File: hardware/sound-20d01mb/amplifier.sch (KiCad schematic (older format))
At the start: 30 parts

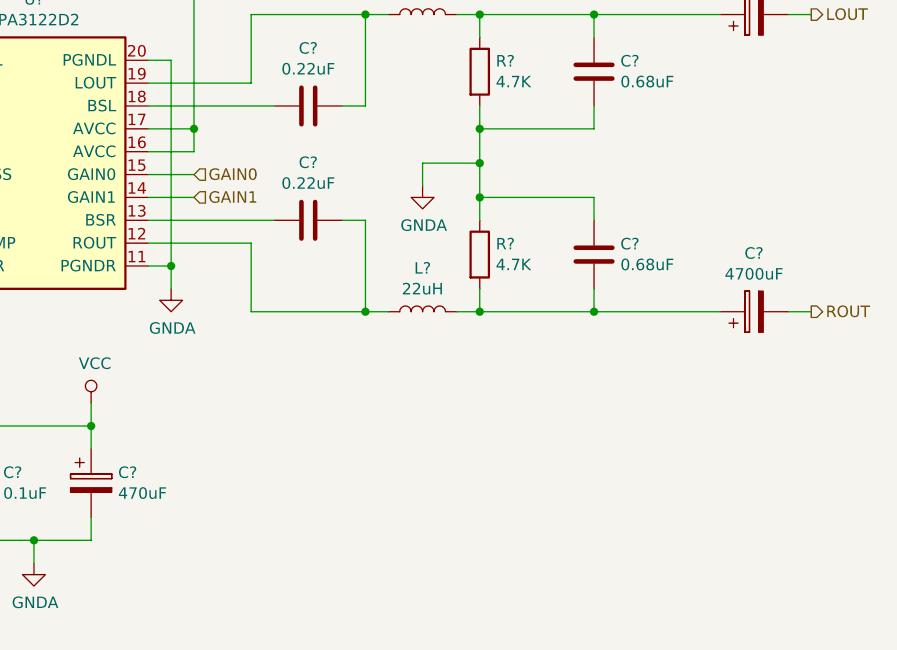
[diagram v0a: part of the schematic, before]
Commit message: Added Gain Settings
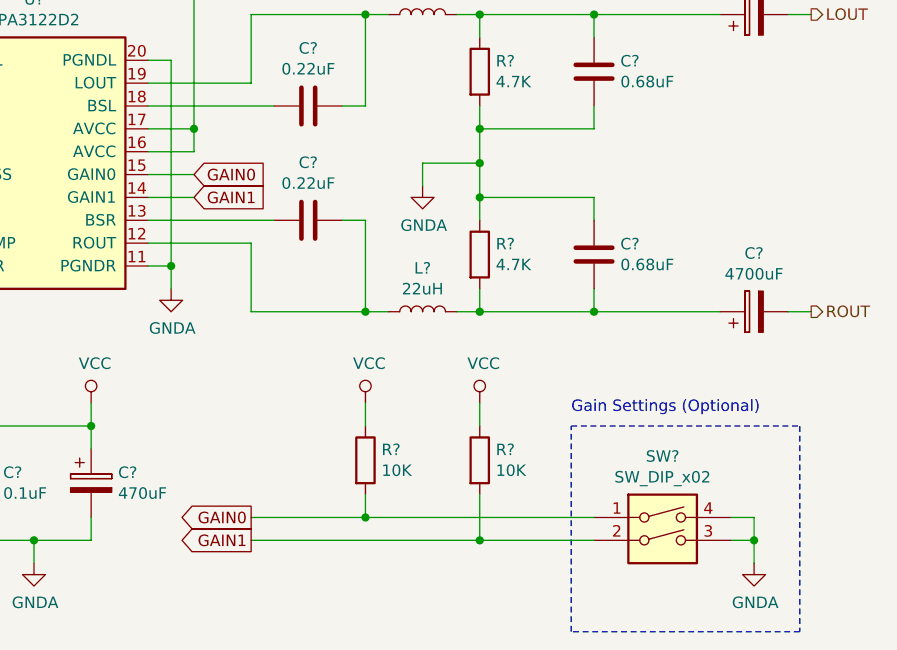
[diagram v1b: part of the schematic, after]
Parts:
- added R? (x2): 10K, Resistor_SMD:R_1206_3216Metric_Pad1.42x1.75mm_HandSolder, symbol Device:R
- added SW?: SW_DIP_x02, Button_Switch_THT:SW_DIP_SPSTx02_Slide_9.78x7.26mm_W7.62mm_P2.54mm, symbol Switch:SW_DIP_x02
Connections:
- net GAIN0: now also R?.2, SW?.1
- net GAIN1: now also R?.2, SW?.2
- net GNDA: now also SW?.3, SW?.4
- net VCC: now also R?.1, R?.1
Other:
- note added: "Gain Settings (Optional)"
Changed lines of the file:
@@
 Connection ~ 8650 2000
-Wire Wire Line
-	7450 3700 7650 3700
-Wire Wire Line
-	7450 3800 7650 3800
 Wire Wire Line
 	7450 3300 7900 3300
@@
 Wire Wire Line
 	6450 3400 6350 3400
-Text HLabel 7650 3700 2    50   Input ~ 0
-GAIN0
-Text HLabel 7650 3800 2    50   Input ~ 0
-GAIN1
 $Comp
 L sound-20d01_Library:PGA2311P U?
@@
 Text Notes 1150 1100 0    50   ~ 0
 Place power-supply bypass capacitors as\nclose to the PGA2311 package as physically possible.
+$Comp
+L Switch:SW_DIP_x02 SW?
+U 1 1 60E21294
+P 9700 5300
+F 0 "SW?" H 9700 5667 50  0000 C CNN
+F 1 "SW_DIP_x02" H 9700 5576 50  0000 C CNN
+F 2 "Button_Switch_THT:SW_DIP_SPSTx02_Slide_9.78x7.26mm_W7.62mm_P2.54mm" H 9700 5300 50  0001 C CNN
+F 3 "" H 9700 5300 50  0001 C CNN
+	1    9700 5300
+	1    0    0    -1
+$EndComp
+$Comp
+L power:GNDA #PWR?
+U 1 1 60E2143D
+P 10100 5400
+F 0 "#PWR?" H 10100 5150 50  0001 C CNN
+F 1 "GNDA" H 10105 5227 50  0000 C CNN
+F 2 "" H 10100 5400 50  0001 C CNN
+F 3 "" H 10100 5400 50  0001 C CNN
+	1    10100 5400
+	1    0    0    -1
+$EndComp
+Wire Wire Line
+	10000 5300 10100 5300
+Wire Wire Line
+	10100 5300 10100 5400
+Wire Wire Line
+	10000 5200 10100 5200
+Wire Wire Line
+	10100 5200 10100 5300
+Connection ~ 10100 5300
+$Comp
+L Device:R R?
+U 1 1 60E3F5FC
+P 8400 4950
+F 0 "R?" H 8470 4996 50  0000 L CNN
+F 1 "10K" H 8470 4905 50  0000 L CNN
+F 2 "Resistor_SMD:R_1206_3216Metric_Pad1.42x1.75mm_HandSolder" V 8330 4950 50  0001 C CNN
+F 3 "~" H 8400 4950 50  0001 C CNN
+	1    8400 4950
+	1    0    0    -1
+$EndComp
+$Comp
+L Device:R R?
+U 1 1 60E56A6D
+P 8900 4950
+F 0 "R?" H 8970 4996 50  0000 L CNN
+F 1 "10K" H 8970 4905 50  0000 L CNN
+F 2 "Resistor_SMD:R_1206_3216Metric_Pad1.42x1.75mm_HandSolder" V 8830 4950 50  0001 C CNN
+F 3 "~" H 8900 4950 50  0001 C CNN
+	1    8900 4950
+	1    0    0    -1
+$EndComp
+$Comp
+L power:VCC #PWR?
+U 1 1 60E7D456
+P 8400 4700
+F 0 "#PWR?" H 8400 4550 50  0001 C CNN
+F 1 "VCC" H 8417 4873 50  0000 C CNN
+F 2 "" H 8400 4700 50  0001 C CNN
+F 3 "" H 8400 4700 50  0001 C CNN
+	1    8400 4700
+	1    0    0    -1
+$EndComp
+Wire Wire Line
+	8400 4800 8400 4700
+$Comp
+L power:VCC #PWR?
+U 1 1 60E84FC2
+P 8900 4700
+F 0 "#PWR?" H 8900 4550 50  0001 C CNN
+F 1 "VCC" H 8917 4873 50  0000 C CNN
+F 2 "" H 8900 4700 50  0001 C CNN
+F 3 "" H 8900 4700 50  0001 C CNN
+	1    8900 4700
+	1    0    0    -1
+$EndComp
+Wire Wire Line
+	8900 4800 8900 4700
+Wire Wire Line
+	9400 5200 8400 5200
+Wire Wire Line
+	8400 5200 8400 5100
+Wire Wire Line
+	9400 5300 8900 5300
+Wire Wire Line
+	8900 5300 8900 5100
+Wire Notes Line
+	9300 4800 10300 4800
+Wire Notes Line
+	10300 4800 10300 5700
+Wire Notes Line
+	10300 5700 9300 5700
+Wire Notes Line
+	9300 5700 9300 4800
+Text Notes 9300 4750 0    50   ~ 0
+Gain Settings (Optional)
+Wire Wire Line
+	7450 3700 7650 3700
+Wire Wire Line
+	7450 3800 7650 3800
+Wire Wire Line
+	8400 5200 7900 5200
+Connection ~ 8400 5200
+Wire Wire Line
+	8900 5300 7900 5300
+Connection ~ 8900 5300
+Text GLabel 7900 5200 0    50   Output ~ 0
+GAIN0
+Text GLabel 7650 3700 2    50   Input ~ 0
+GAIN0
+Text GLabel 7900 5300 0    50   Output ~ 0
+GAIN1
+Text GLabel 7650 3800 2    50   Input ~ 0
+GAIN1
 $EndSCHEMATC

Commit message: Connected MCU to DAC
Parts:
- C? (x4): footprint (none) -> Capacitor_SMD:C_1206_3216Metric_Pad1.42x1.75mm_HandSolder
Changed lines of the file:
@@
 F 0 "C?" V 5102 3300 50  0000 C CNN
 F 1 "2.2uF" V 5011 3300 50  0000 C CNN
-F 2 "" H 4888 3150 50  0001 C CNN
+F 2 "Capacitor_SMD:C_1206_3216Metric_Pad1.42x1.75mm_HandSolder" H 4888 3150 50  0001 C CNN
 F 3 "~" H 4850 3300 50  0001 C CNN
 	1    4850 3300
@@
 F 0 "C?" V 5102 3800 50  0000 C CNN
 F 1 "2.2uF" V 5011 3800 50  0000 C CNN
-F 2 "" H 4888 3650 50  0001 C CNN
+F 2 "Capacitor_SMD:C_1206_3216Metric_Pad1.42x1.75mm_HandSolder" H 4888 3650 50  0001 C CNN
 F 3 "~" H 4850 3800 50  0001 C CNN
 	1    4850 3800
@@
 F 0 "C?" V 4152 4100 50  0000 C CNN
 F 1 "2.2uF" V 4061 4100 50  0000 C CNN
-F 2 "" H 3938 3950 50  0001 C CNN
+F 2 "Capacitor_SMD:C_1206_3216Metric_Pad1.42x1.75mm_HandSolder" H 3938 3950 50  0001 C CNN
 F 3 "~" H 3900 4100 50  0001 C CNN
 	1    3900 4100
@@
 F 0 "C?" V 4152 3000 50  0000 C CNN
 F 1 "2.2uF" V 4061 3000 50  0000 C CNN
-F 2 "" H 3938 2850 50  0001 C CNN
+F 2 "Capacitor_SMD:C_1206_3216Metric_Pad1.42x1.75mm_HandSolder" H 3938 2850 50  0001 C CNN
 F 3 "~" H 3900 3000 50  0001 C CNN
 	1    3900 3000

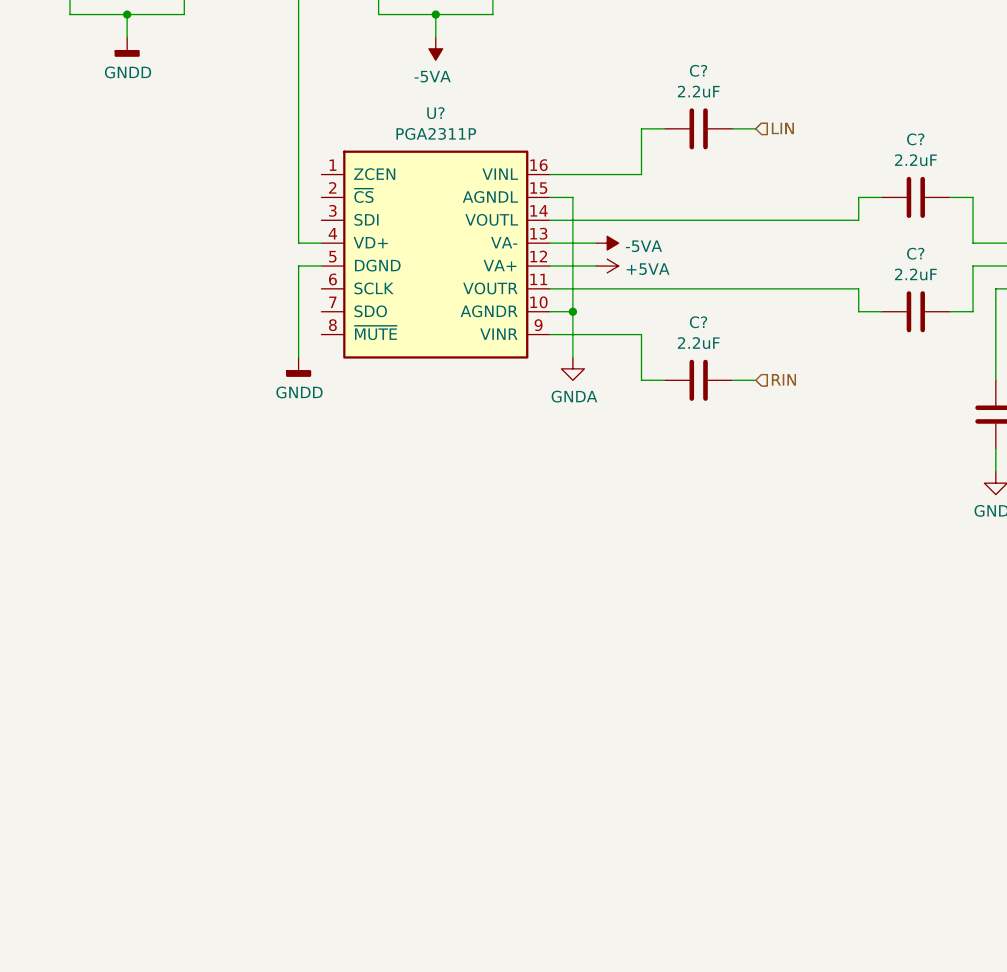
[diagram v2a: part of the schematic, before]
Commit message: Added ADG3304BRUZ
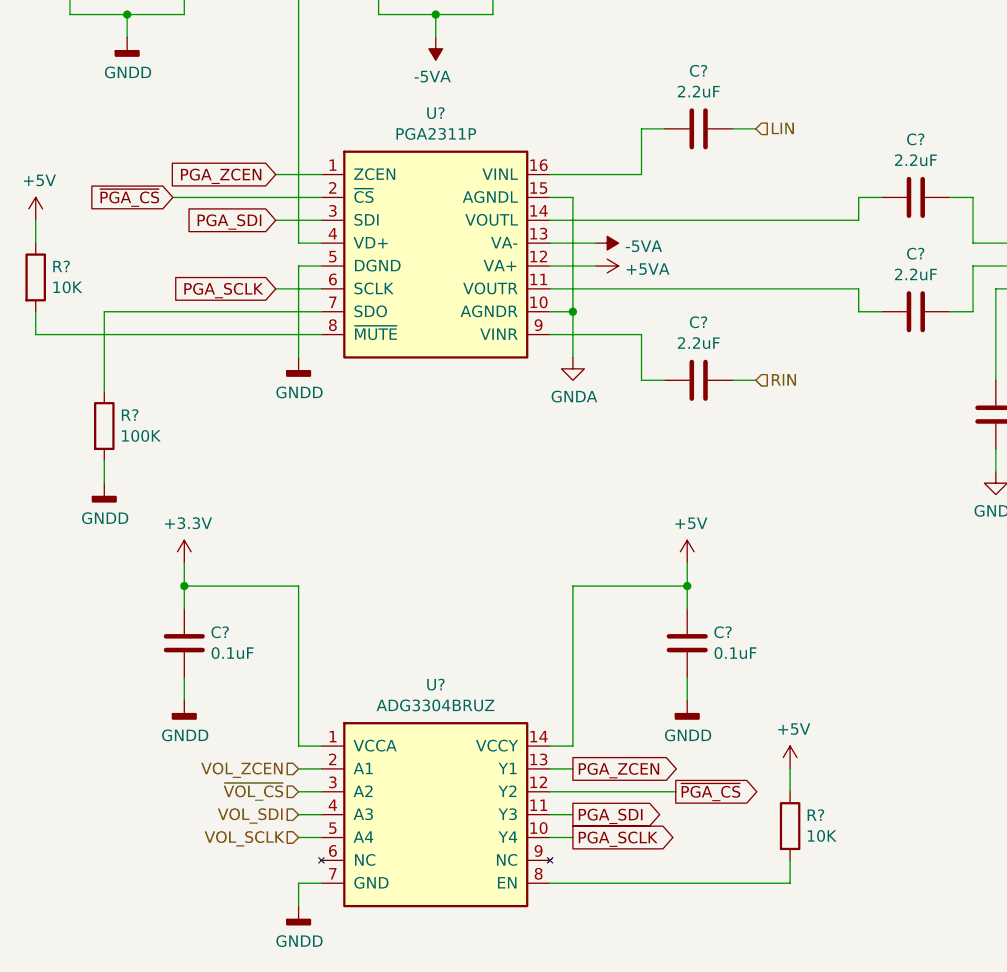
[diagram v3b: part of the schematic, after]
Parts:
- added C? (x2): 0.1uF, Capacitor_SMD:C_1206_3216Metric_Pad1.42x1.75mm_HandSolder, symbol Device:C
- added R?: 100K, Resistor_SMD:R_1206_3216Metric_Pad1.42x1.75mm_HandSolder, symbol Device:R
- added R? (x2): 10K, Resistor_SMD:R_1206_3216Metric_Pad1.42x1.75mm_HandSolder, symbol Device:R
- added U?: ADG3304BRUZ, Package_SO:TSSOP-14_4.4x5mm_P0.65mm, symbol sound-20d01_Library:ADG3304BRUZ
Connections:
- net +5V: now also C?.1, R?.1, R?.1, U?.14 (VCCY)
- net GNDD: now also C?.2, C?.2, R?.2, U?.7 (GND)
- net PGA_ZCEN: now reaches U?.1 (ZCEN)
- net PGA_ZCEN: now also U?.13 (Y1)
- net ~PGA_CS: now reaches U?.2 (~CS)
- net ~PGA_CS: now also U?.12 (Y2)
- net PGA_SDI: now reaches U?.3 (SDI)
- net PGA_SDI: now also U?.11 (Y3)
- net PGA_SCLK: now reaches U?.6 (SCLK)
- net PGA_SCLK: now also U?.10 (Y4)
- net at U?.7 (SDO): now also R?.1
- net at U?.8 (~MUTE): now also R?.2
- new net: R?.2, U?.8 (EN)
- new net +3V3: C?.1, U?.1 (VCCA)
- new net VOL_SCLK: U?.5 (A4)
- new net VOL_SDI: U?.4 (A3)
- new net VOL_ZCEN: U?.2 (A1)
- new net ~VOL_CS: U?.3 (A2)

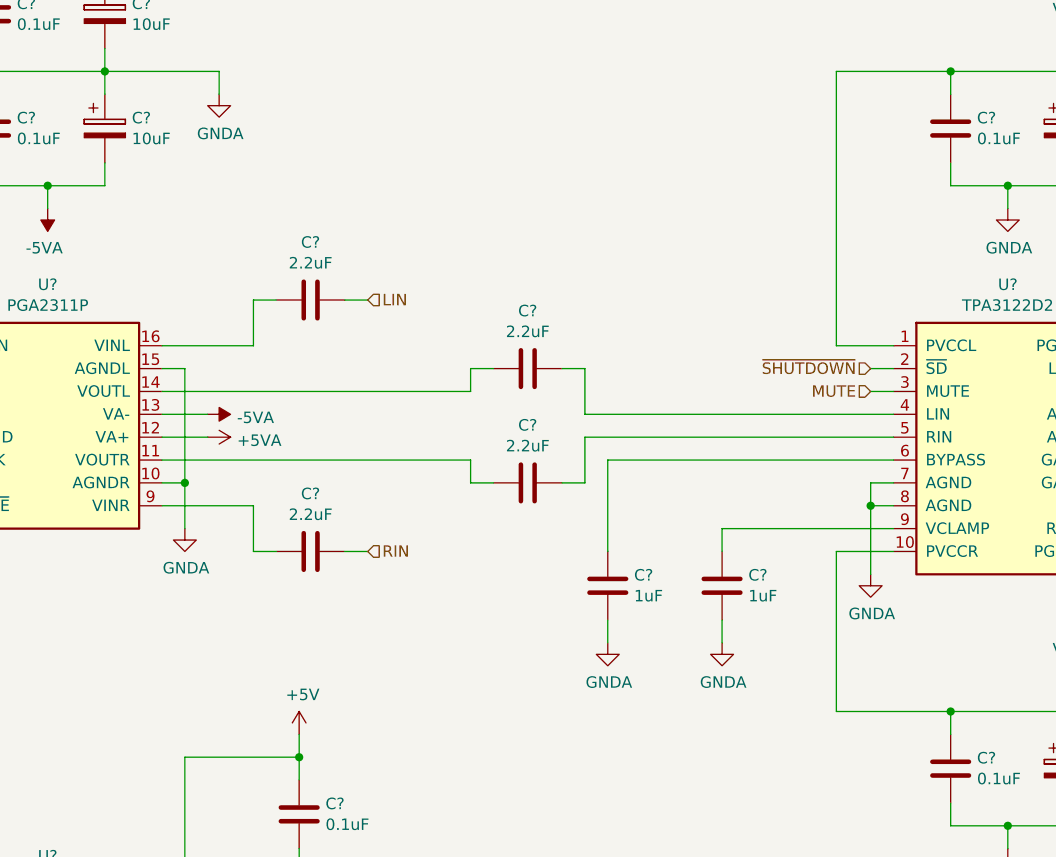
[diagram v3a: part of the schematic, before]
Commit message: Updated amplifier.sch
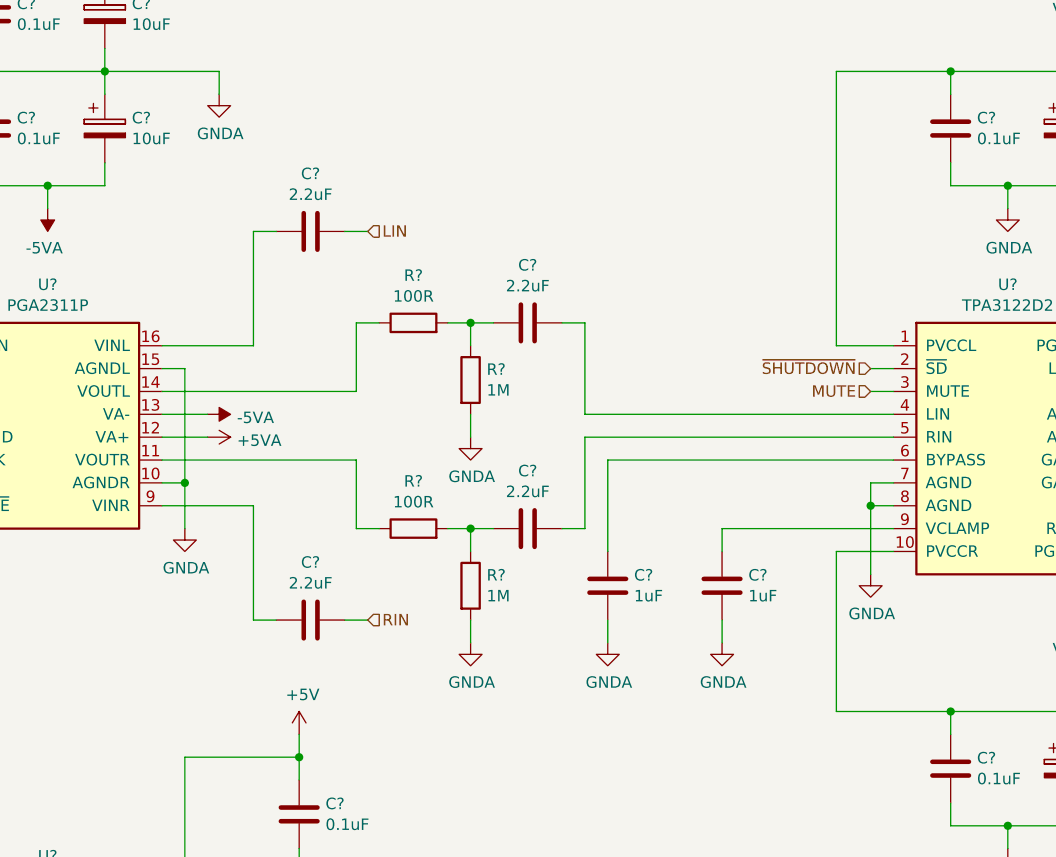
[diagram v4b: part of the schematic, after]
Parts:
- added R? (x2): 100R, Resistor_SMD:R_1206_3216Metric_Pad1.42x1.75mm_HandSolder, symbol Device:R
- added R? (x2): 1M, Resistor_SMD:R_1206_3216Metric_Pad1.42x1.75mm_HandSolder, symbol Device:R
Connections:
- net GNDA: now also R?.2, R?.2
- net at U?.11 (VOUTR): now also R?.1; no longer C?.1
- net at U?.14 (VOUTL): now also R?.1; no longer C?.1
- new net: C?.1, R?.1, R?.2 (x2)
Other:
- moved on the sheet: C?
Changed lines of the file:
@@
 L Device:C C?
 U 1 1 60E76A1B
-P 4850 3300
-F 0 "C?" V 5102 3300 50  0000 C CNN
-F 1 "2.2uF" V 5011 3300 50  0000 C CNN
-F 2 "Capacitor_SMD:C_1206_3216Metric_Pad1.42x1.75mm_HandSolder" H 4888 3150 50  0001 C CNN
-F 3 "~" H 4850 3300 50  0001 C CNN
-	1    4850 3300
+P 4850 3100
+F 0 "C?" V 5102 3100 50  0000 C CNN
+F 1 "2.2uF" V 5011 3100 50  0000 C CNN
+F 2 "Capacitor_SMD:C_1206_3216Metric_Pad1.42x1.75mm_HandSolder" H 4888 2950 50  0001 C CNN
+F 3 "~" H 4850 3100 50  0001 C CNN
+	1    4850 3100
 	0    -1   -1   0
 $EndComp
@@
 L Device:C C?
 U 1 1 60E79504
-P 4850 3800
-F 0 "C?" V 5102 3800 50  0000 C CNN
-F 1 "2.2uF" V 5011 3800 50  0000 C CNN
-F 2 "Capacitor_SMD:C_1206_3216Metric_Pad1.42x1.75mm_HandSolder" H 4888 3650 50  0001 C CNN
-F 3 "~" H 4850 3800 50  0001 C CNN
-	1    4850 3800
+P 4850 4000
+F 0 "C?" V 5102 4000 50  0000 C CNN
+F 1 "2.2uF" V 5011 4000 50  0000 C CNN
+F 2 "Capacitor_SMD:C_1206_3216Metric_Pad1.42x1.75mm_HandSolder" H 4888 3850 50  0001 C CNN
+F 3 "~" H 4850 4000 50  0001 C CNN
+	1    4850 4000
 	0    -1   -1   0
 $EndComp
-Wire Wire Line
-	6450 3600 5100 3600
-Wire Wire Line
-	6450 3500 5100 3500
-Wire Wire Line
-	5100 3500 5100 3300
-Wire Wire Line
-	5100 3300 5000 3300
-Wire Wire Line
-	5100 3600 5100 3800
-Wire Wire Line
-	5100 3800 5000 3800
-Text HLabel 4150 3000 2    50   Input ~ 0
+Text HLabel 4150 2700 2    50   Input ~ 0
 LIN
-Text HLabel 4150 4100 2    50   Input ~ 0
+Text HLabel 4150 4400 2    50   Input ~ 0
 RIN
 Text HLabel 10350 3000 2    50   Output ~ 0
@@
 $EndComp
 Wire Wire Line
-	4600 3400 4600 3300
-Wire Wire Line
-	4600 3300 4700 3300
-Wire Wire Line
-	4600 3700 4600 3800
-Wire Wire Line
-	4600 3800 4700 3800
-Wire Wire Line
 	2150 3500 2150 2000
 $Comp
 L Device:C C?
 U 1 1 610438D7
-P 3900 4100
-F 0 "C?" V 4152 4100 50  0000 C CNN
-F 1 "2.2uF" V 4061 4100 50  0000 C CNN
-F 2 "Capacitor_SMD:C_1206_3216Metric_Pad1.42x1.75mm_HandSolder" H 3938 3950 50  0001 C CNN
-F 3 "~" H 3900 4100 50  0001 C CNN
-	1    3900 4100
+P 3900 4400
+F 0 "C?" V 4152 4400 50  0000 C CNN
+F 1 "2.2uF" V 4061 4400 50  0000 C CNN
+F 2 "Capacitor_SMD:C_1206_3216Metric_Pad1.42x1.75mm_HandSolder" H 3938 4250 50  0001 C CNN
+F 3 "~" H 3900 4400 50  0001 C CNN
+	1    3900 4400
 	0    -1   -1   0
 $EndComp
-Wire Wire Line
-	4150 4100 4050 4100
-Wire Wire Line
-	3750 4100 3650 4100
-Wire Wire Line
-	3650 4100 3650 3900
-Wire Wire Line
-	3250 3900 3650 3900
-Wire Wire Line
-	3250 3200 3650 3200
-Wire Wire Line
-	3650 3200 3650 3000
 $Comp
 L Device:C C?
 U 1 1 610670CA
-P 3900 3000
-F 0 "C?" V 4152 3000 50  0000 C CNN
-F 1 "2.2uF" V 4061 3000 50  0000 C CNN
-F 2 "Capacitor_SMD:C_1206_3216Metric_Pad1.42x1.75mm_HandSolder" H 3938 2850 50  0001 C CNN
-F 3 "~" H 3900 3000 50  0001 C CNN
-	1    3900 3000
+P 3900 2700
+F 0 "C?" V 4152 2700 50  0000 C CNN
+F 1 "2.2uF" V 4061 2700 50  0000 C CNN
+F 2 "Capacitor_SMD:C_1206_3216Metric_Pad1.42x1.75mm_HandSolder" H 3938 2550 50  0001 C CNN
+F 3 "~" H 3900 2700 50  0001 C CNN
+	1    3900 2700
 	0    -1   -1   0
 $EndComp
-Wire Wire Line
-	4150 3000 4050 3000
-Wire Wire Line
-	3750 3000 3650 3000
-Wire Wire Line
-	4600 3400 3250 3400
-Wire Wire Line
-	4600 3700 3250 3700
 Text Notes 1150 1100 0    50   ~ 0
 Place power-supply bypass capacitors as\nclose to the PGA2311 package as physically possible.
@@
 Wire Wire Line
 	1000 3900 1000 3800
+$Comp
+L Device:R R?
+U 1 1 60E774AC
+P 4350 3100
+F 0 "R?" V 4557 3100 50  0000 C CNN
+F 1 "100R" V 4466 3100 50  0000 C CNN
+F 2 "Resistor_SMD:R_1206_3216Metric_Pad1.42x1.75mm_HandSolder" V 4280 3100 50  0001 C CNN
+F 3 "~" H 4350 3100 50  0001 C CNN
+	1    4350 3100
+	0    -1   -1   0
+$EndComp
+$Comp
+L Device:R R?
+U 1 1 60E83DCC
+P 4350 4000
+F 0 "R?" V 4557 4000 50  0000 C CNN
+F 1 "100R" V 4466 4000 50  0000 C CNN
+F 2 "Resistor_SMD:R_1206_3216Metric_Pad1.42x1.75mm_HandSolder" V 4280 4000 50  0001 C CNN
+F 3 "~" H 4350 4000 50  0001 C CNN
+	1    4350 4000
+	0    -1   -1   0
+$EndComp
+$Comp
+L Device:R R?
+U 1 1 60EBA10D
+P 4600 4250
+F 0 "R?" H 4670 4296 50  0000 L CNN
+F 1 "1M" H 4670 4205 50  0000 L CNN
+F 2 "Resistor_SMD:R_1206_3216Metric_Pad1.42x1.75mm_HandSolder" V 4530 4250 50  0001 C CNN
+F 3 "~" H 4600 4250 50  0001 C CNN
+	1    4600 4250
+	1    0    0    -1
+$EndComp
+$Comp
+L power:GNDA #PWR?
+U 1 1 60EDFC4C
+P 4600 4500
+F 0 "#PWR?" H 4600 4250 50  0001 C CNN
+F 1 "GNDA" H 4605 4327 50  0000 C CNN
+F 2 "" H 4600 4500 50  0001 C CNN
+F 3 "" H 4600 4500 50  0001 C CNN
+	1    4600 4500
+	1    0    0    -1
+$EndComp
+Wire Wire Line
+	4600 4400 4600 4500
+$Comp
+L Device:R R?
+U 1 1 60F53986
+P 4600 3350
+F 0 "R?" H 4670 3396 50  0000 L CNN
+F 1 "1M" H 4670 3305 50  0000 L CNN
+F 2 "Resistor_SMD:R_1206_3216Metric_Pad1.42x1.75mm_HandSolder" V 4530 3350 50  0001 C CNN
+F 3 "~" H 4600 3350 50  0001 C CNN
+	1    4600 3350
+	1    0    0    -1
+$EndComp
+$Comp
+L power:GNDA #PWR?
+U 1 1 60F5398D
+P 4600 3600
+F 0 "#PWR?" H 4600 3350 50  0001 C CNN
+F 1 "GNDA" H 4605 3427 50  0000 C CNN
+F 2 "" H 4600 3600 50  0001 C CNN
+F 3 "" H 4600 3600 50  0001 C CNN
+	1    4600 3600
+	1    0    0    -1
+$EndComp
+Wire Wire Line
+	4600 3500 4600 3600
+Wire Wire Line
+	3250 3200 3650 3200
+Wire Wire Line
+	3650 3200 3650 2700
+Wire Wire Line
+	3650 2700 3750 2700
+Wire Wire Line
+	3250 3900 3650 3900
+Wire Wire Line
+	3650 3900 3650 4400
+Wire Wire Line
+	3650 4400 3750 4400
+Wire Wire Line
+	4150 2700 4050 2700
+Wire Wire Line
+	4150 4400 4050 4400
+Wire Wire Line
+	3250 3400 4100 3400
+Wire Wire Line
+	4100 3400 4100 3100
+Wire Wire Line
+	4100 3100 4200 3100
+Wire Wire Line
+	4500 3100 4600 3100
+Wire Wire Line
+	4600 3100 4600 3200
+Connection ~ 4600 3100
+Wire Wire Line
+	4600 3100 4700 3100
+Wire Wire Line
+	5000 3100 5100 3100
+Wire Wire Line
+	5100 3100 5100 3500
+Wire Wire Line
+	5100 3500 6450 3500
+Wire Wire Line
+	3250 3700 4100 3700
+Wire Wire Line
+	4100 3700 4100 4000
+Wire Wire Line
+	4100 4000 4200 4000
+Wire Wire Line
+	4500 4000 4600 4000
+Wire Wire Line
+	4600 4000 4600 4100
+Connection ~ 4600 4000
+Wire Wire Line
+	4600 4000 4700 4000
+Wire Wire Line
+	5000 4000 5100 4000
+Wire Wire Line
+	5100 4000 5100 3600
+Wire Wire Line
+	5100 3600 6450 3600
 $EndSCHEMATC
